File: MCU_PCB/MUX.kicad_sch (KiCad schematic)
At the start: 21 parts

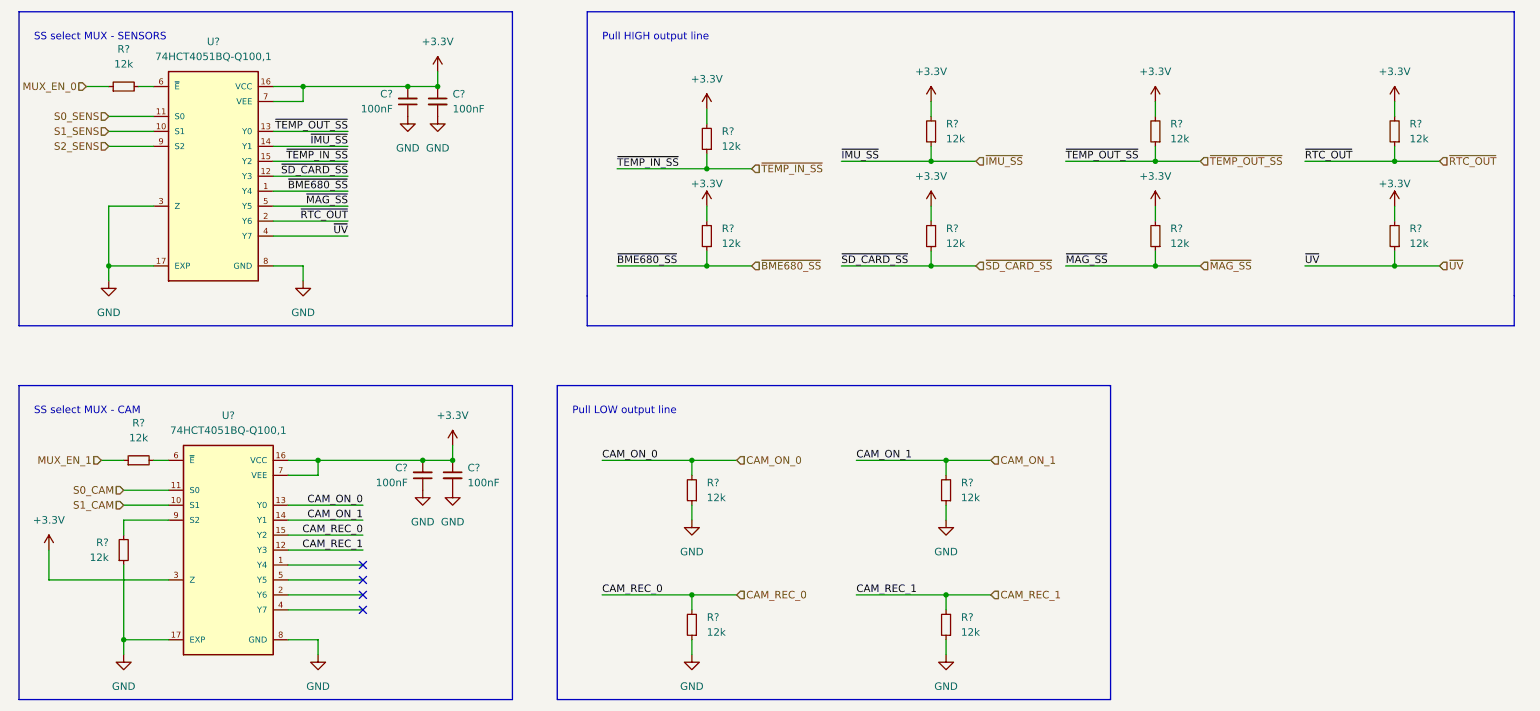
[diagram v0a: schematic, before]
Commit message: 0.1v MCU KiCad
Aesthetics needs to be improved.
Trace width needs to be changed.
More sufficient grounding.
Component placement could be changed.
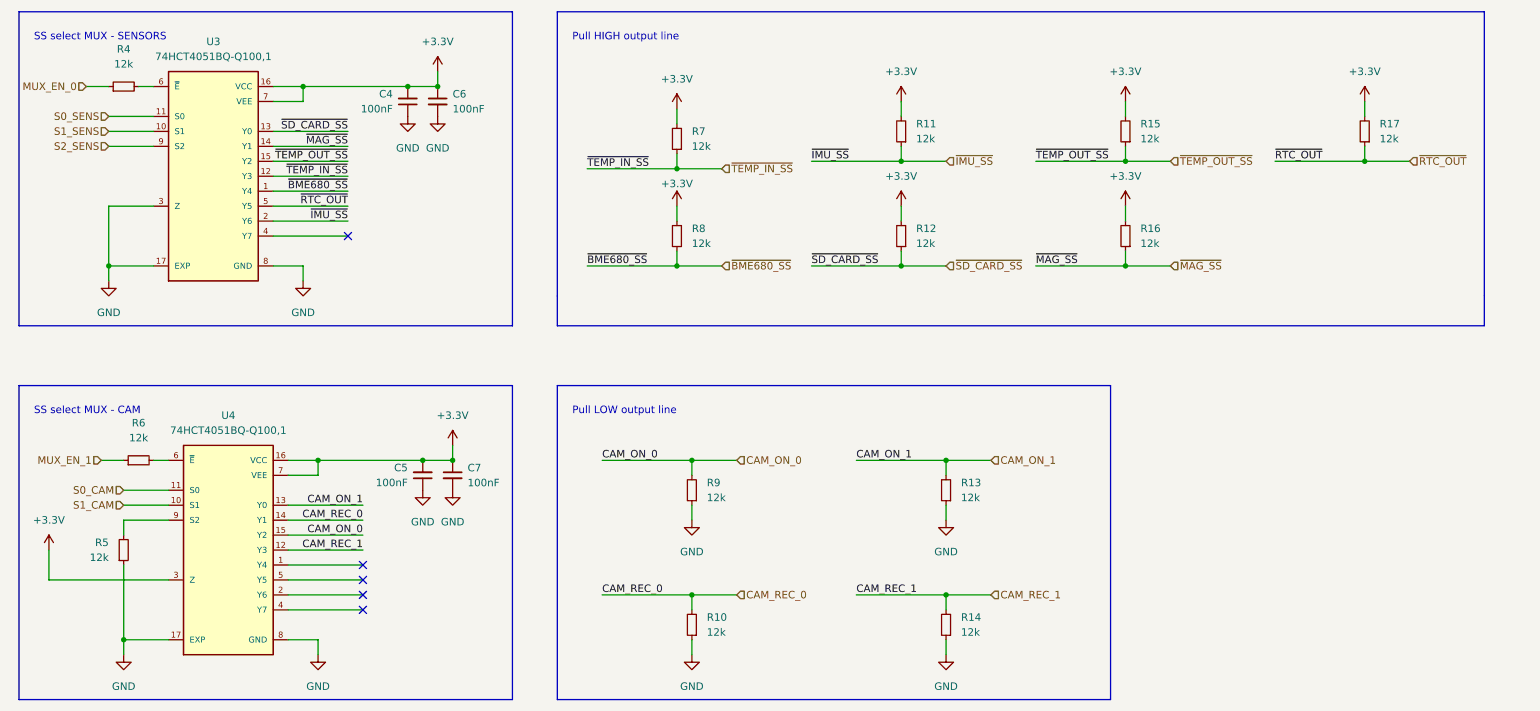
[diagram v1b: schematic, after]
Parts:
- removed R?: 12k, symbol Device:R_Small
- C4, C5, C6, C7: renamed from C?; footprint (none) -> Capacitor_SMD:C_0402_1005Metric
- R10, R11, R12, R13, R14, R15, R16, R17, R4, R5, R6, R7, R8, R9: renamed from R?; footprint (none) -> Resistor_SMD:R_0402_1005Metric
- gave numbers to parts that had none: 2
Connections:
- net CAM_ON_0: now also U4.15 (Y2); no longer U4.13 (Y0)
- net CAM_ON_1: now also U4.13 (Y0); no longer U4.14 (Y1)
- net CAM_REC_0: now also U4.14 (Y1); no longer U4.15 (Y2)
- net ~{IMU_SS}: now also U3.2 (Y6); no longer U3.14 (Y1)
- net ~{MAG_SS}: now also U3.14 (Y1); no longer U3.5 (Y5)
- net ~{RTC_OUT}: now also U3.5 (Y5); no longer U3.2 (Y6)
- net ~{SD_CARD_SS}: now also U3.13 (Y0); no longer U3.12 (Y3)
- net ~{TEMP_IN_SS}: now also U3.12 (Y3); no longer U3.15 (Y2)
- net ~{TEMP_OUT_SS}: now also U3.15 (Y2); no longer U3.13 (Y0)
- net ~{UV}: no longer names the net of U3.4 (Y7)
- no-connect marks 4 -> 5
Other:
- moved on the sheet: R11, R12, R15, R16, R17, R7, R8
